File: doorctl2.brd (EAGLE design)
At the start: 50.8 x 71.1 mm, 48 parts, among them IC1 MEGA8-P, IC2 AT24CP, Q1 FDS5680, Q2 FDS5680, Q3 FDS5680, Q4 FDS5680, SW1 L202011MS02Q, SW2 L202011MS02Q

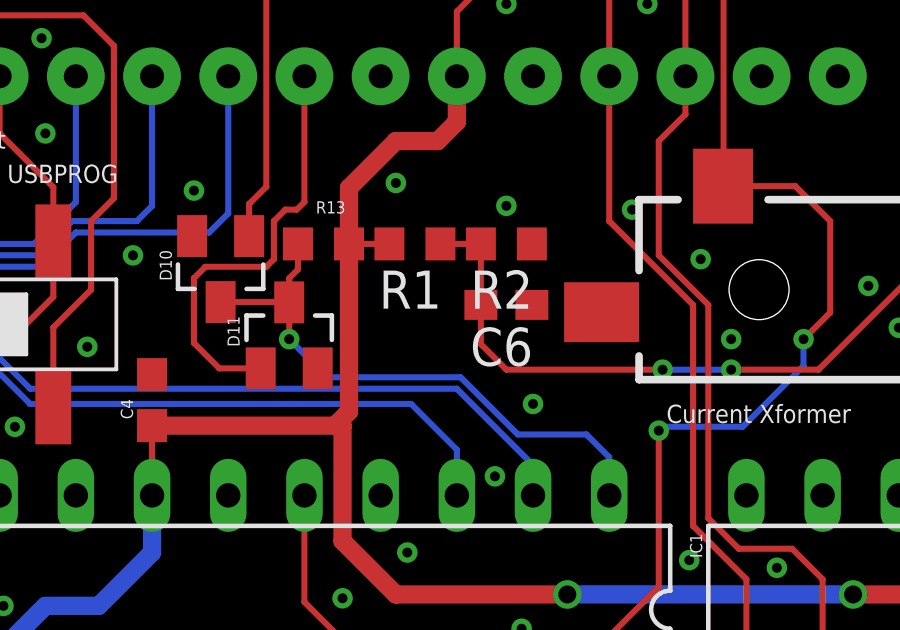
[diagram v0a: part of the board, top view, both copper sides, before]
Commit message: Added Zener to sense xformer input
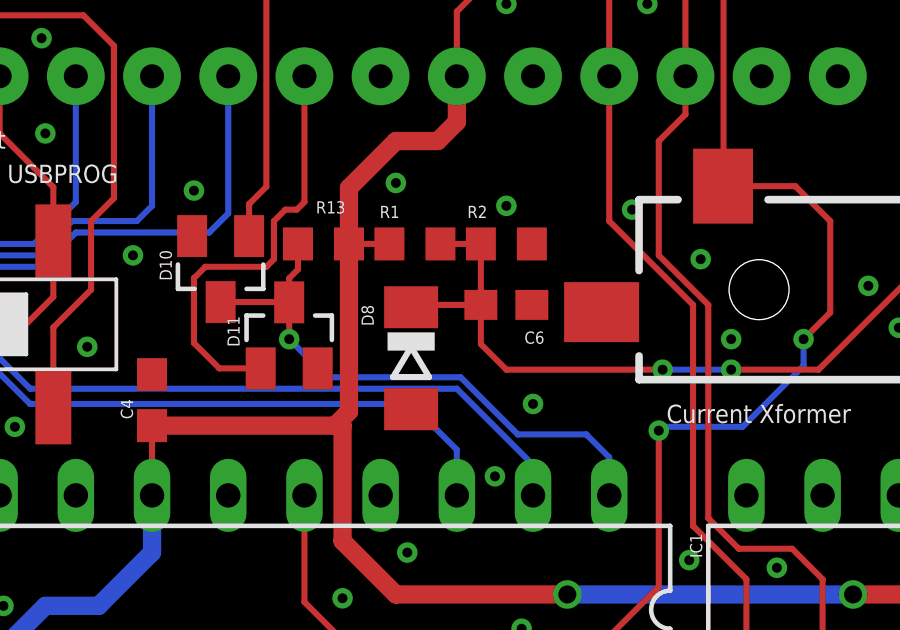
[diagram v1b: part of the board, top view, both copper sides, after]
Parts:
- added D8: (no value), diode:SOD80C
- C1: value (none) -> 4.7uF
- C2: value (none) -> 1uF
- C3, C4, C5: value 130pf -> 1uF
- R14: value 33 -> 330
- R3, R4: value 33 -> 10k
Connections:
- net GND: now also D8.A
- net N$12: now also D8.C
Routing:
- net N$12: track 24.9 -> 27.3 mm
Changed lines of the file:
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@@
 <attribute name="VALUE" x="35.56" y="-0.381" size="1.27" layer="27" ratio="10"/>
 </element>
-<element name="C3" library="rcl" package="C0603" value="130pf" x="47.752" y="15.621" smashed="yes" rot="R270">
+<element name="C3" library="rcl" package="C0603" value="1uF" x="47.752" y="15.621" smashed="yes" rot="R270">
 <attribute name="NAME" x="48.387" y="16.256" size="0.4064" layer="25" font="vector" rot="R270"/>
 <attribute name="VALUE" x="47.498" y="16.637" size="0.4064" layer="27" font="vector" rot="R270"/>
@@
 <attribute name="VALUE" x="8.763" y="12.319" size="1.27" layer="27"/>
 </element>
-<element name="C1" library="rcl" package="C0805" value="" x="8.636" y="57.912" smashed="yes">
+<element name="C1" library="rcl" package="C0805" value="4.7uF" x="8.636" y="57.912" smashed="yes">
 <attribute name="NAME" x="6.477" y="58.166" size="0.4064" layer="25" font="vector" rot="R90"/>
 <attribute name="VALUE" x="7.366" y="55.372" size="1.27" layer="27"/>
 </element>
-<element name="C2" library="rcl" package="C0805" value="" x="8.636" y="55.88" smashed="yes">
+<element name="C2" library="rcl" package="C0805" value="1uF" x="8.636" y="55.88" smashed="yes">
 <attribute name="NAME" x="6.477" y="56.134" size="0.4064" layer="25" font="vector" rot="R90"/>
 <attribute name="VALUE" x="7.366" y="53.34" size="1.27" layer="27"/>
 </element>
-<element name="C4" library="rcl" package="C0603" value="130pf" x="20.32" y="29.845" smashed="yes" rot="R90">
+<element name="C4" library="rcl" package="C0603" value="1uF" x="20.32" y="29.845" smashed="yes" rot="R90">
 <attribute name="NAME" x="19.685" y="29.21" size="0.4064" layer="25" font="vector" rot="R90"/>
 <attribute name="VALUE" x="20.447" y="28.956" size="0.4064" layer="27" font="vector" rot="R90"/>
 </element>
-<element name="C5" library="rcl" package="C0603" value="130pf" x="18.034" y="16.51" smashed="yes">
+<element name="C5" library="rcl" package="C0603" value="1uF" x="18.034" y="16.51" smashed="yes">
 <attribute name="NAME" x="17.399" y="17.145" size="0.4064" layer="25" font="vector"/>
 <attribute name="VALUE" x="17.272" y="16.256" size="0.4064" layer="27" font="vector"/>
@@
 <attribute name="VALUE" x="14.224" y="12.319" size="1.27" layer="27"/>
 </element>
-<element name="R14" library="rcl" package="R0603" value="33" x="18.034" y="14.224" smashed="yes">
+<element name="R14" library="rcl" package="R0603" value="330" x="18.034" y="14.224" smashed="yes">
 <attribute name="NAME" x="17.145" y="15.113" size="0.4064" layer="25" font="vector"/>
 <attribute name="VALUE" x="17.653" y="13.97" size="0.4064" layer="27" font="vector"/>
@@
 <element name="SW2" library="JS202011SCQNC&amp;K" package="SMT" value="L202011MS02Q" x="11.43" y="28.321" smashed="yes"/>
 <element name="SW1" library="JS202011SCQNC&amp;K" package="SMT" value="L202011MS02Q" x="2.032" y="28.321" smashed="yes"/>
-<element name="R1" library="rcl" package="R0603" value="10k" x="29.083" y="35.052" rot="R180"/>
-<element name="R2" library="rcl" package="R0603" value="10k" x="32.131" y="35.052" rot="R180"/>
-<element name="C6" library="rcl" package="C0603" value="0.1uF" x="32.131" y="33.02" rot="R180"/>
+<element name="R1" library="rcl" package="R0603" value="10k" x="29.083" y="35.052" smashed="yes" rot="R180">
+<attribute name="NAME" x="28.575" y="36.322" size="0.4064" layer="25" font="vector" rot="R180"/>
+<attribute name="VALUE" x="29.972" y="37.084" size="1.27" layer="27" rot="R180"/>
+</element>
+<element name="R2" library="rcl" package="R0603" value="10k" x="32.131" y="35.052" smashed="yes" rot="R180">
+<attribute name="NAME" x="31.496" y="36.322" size="0.4064" layer="25" font="vector" rot="R180"/>
+<attribute name="VALUE" x="33.02" y="37.084" size="1.27" layer="27" rot="R180"/>
+</element>
+<element name="C6" library="rcl" package="C0603" value="0.1uF" x="32.131" y="33.02" smashed="yes" rot="R180">
+<attribute name="NAME" x="33.401" y="32.131" size="0.4064" layer="25" font="vector" rot="R180"/>
+<attribute name="VALUE" x="33.02" y="35.052" size="1.27" layer="27" rot="R180"/>
+</element>
 <element name="JP1" library="SparkFun-Connectors" package="AUDIO-JACK-3.5MM-SMD" value="" x="51.054" y="33.528" rot="R180">
 <attribute name="PROD_ID" value="CONN-10353" x="51.054" y="49.022" size="0.4064" layer="27" font="vector" rot="R180" display="off"/>
 </element>
-<element name="R3" library="rcl" package="R0603" value="33" x="38.1" y="46.228" rot="R90"/>
-<element name="R4" library="rcl" package="R0603" value="33" x="35.56" y="46.228" rot="R90"/>
+<element name="R3" library="rcl" package="R0603" value="10k" x="38.1" y="46.228" rot="R90"/>
+<element name="R4" library="rcl" package="R0603" value="10k" x="35.56" y="46.228" rot="R90"/>
+<element name="D8" library="diode" package="SOD80C" value="" x="28.956" y="31.242" smashed="yes" rot="R270">
+<attribute name="NAME" x="27.305" y="33.02" size="0.4064" layer="25" font="vector" rot="R270"/>
+<attribute name="VALUE" x="26.543" y="32.766" size="1.27" layer="27" rot="R270"/>
+</element>
 </elements>
 <signals>
@@
 <via x="45.212" y="32.258" extent="1-16" drill="0.3302" diameter="0.508"/>
 <via x="49.53" y="34.798" extent="1-16" drill="0.3302" diameter="0.508"/>
+<contactref element="D8" pad="A"/>
 </signal>
 <signal name="ESP_TX">
@@
 <wire x1="32.131" y1="30.861" x2="31.281" y2="31.711" width="0.2032" layer="1"/>
 <wire x1="31.281" y1="31.711" x2="31.281" y2="33.02" width="0.2032" layer="1"/>
+<contactref element="D8" pad="C"/>
+<wire x1="28.956" y1="32.942" x2="29.034" y2="33.02" width="0.2032" layer="1"/>
+<wire x1="29.034" y1="33.02" x2="31.281" y2="33.02" width="0.2032" layer="1"/>
 </signal>
 <signal name="CURR">
